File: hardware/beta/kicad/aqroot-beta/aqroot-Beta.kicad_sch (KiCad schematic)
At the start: 0 parts

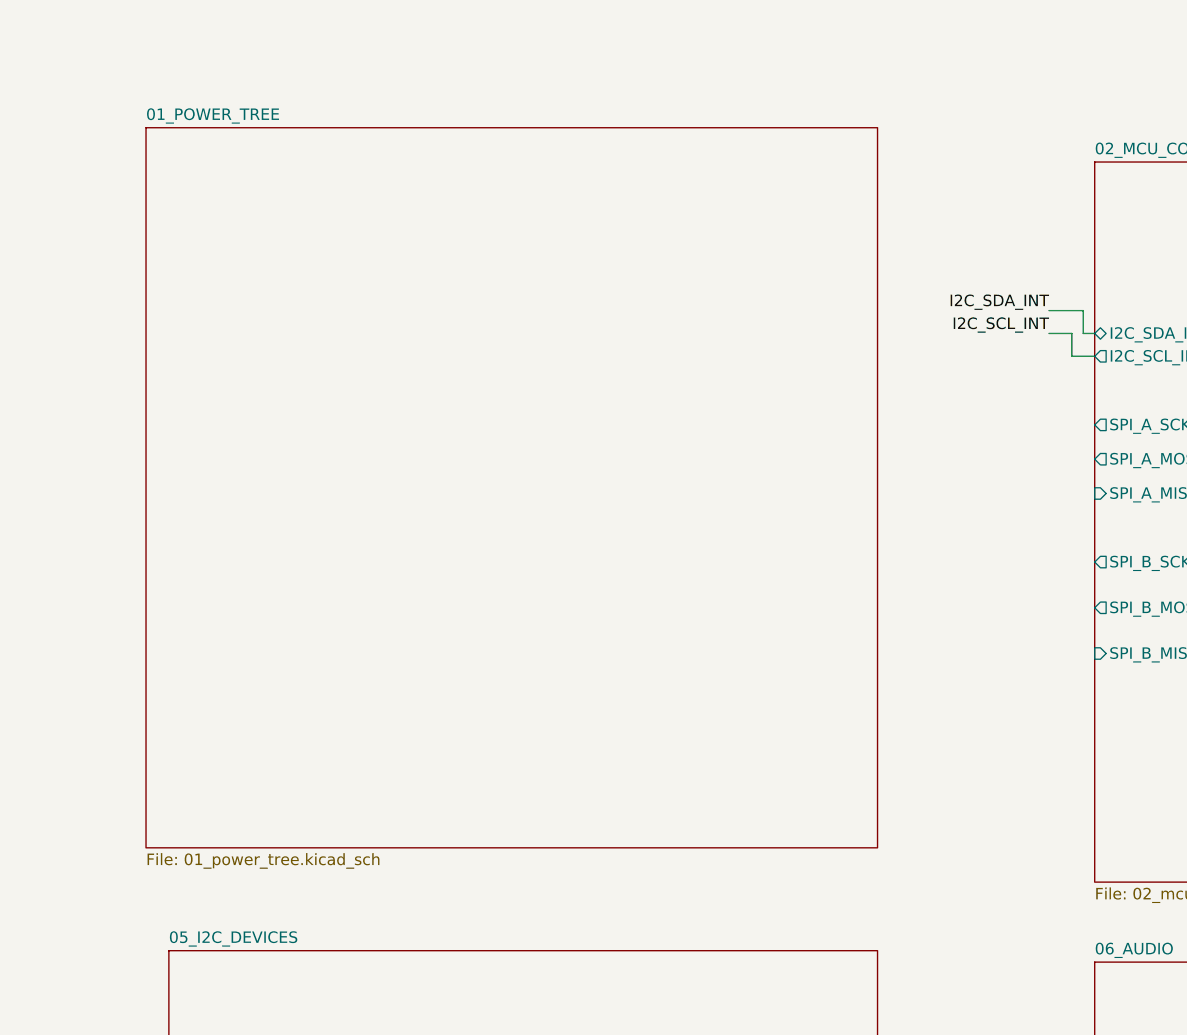
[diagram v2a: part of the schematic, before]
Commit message: AQROOT Beta: finish power-tree integration and add community-header connector map
01_POWER_TREE:
- Wire MAX17048 fuel gauge (U14): VDD/CELL to BAT_PROTECTED_P, GND/EP/CTG
  to GND, SCL to I2C_SCL_INT, SDA to I2C_SDA_INT, QSTRT no-connect.
- Add C36 bulk cap on BAT_PROTECTED_P and TP11 test point on MAX17048_ALRT_N.
- Add 8 hierarchical labels: USB_D_N_MCU, USB_D_P_MCU, I2C_SDA_INT,
  I2C_SCL_INT, NFC_5V_EN, NFC_5V_PA_PENDING, BQ25185_SYS, BAT_PROTECTED_P.

Root sheet:
- Import the 8 matching 01_POWER_TREE sheet pins and name six of them at
  root level, promoting BQ25185_SYS, BAT_PROTECTED_P, NFC_5V_EN,
  USB_D_N_MCU and USB_D_P_MCU from sheet-local to root nets.

09_COMMUNITY_HEADER:
- Add J5 (Conn_02x13_Odd_Even, PinHeader_2x13_P2.54mm_Vertical) with the
  full 26-pin map, plus orientation and 3.3V-only warning notes.

04_SPI_B_RADIOS_NFC:
- KiCad de-duplicated two colliding pin UUIDs on C19 (the file carried each
  UUID twice); included because it is a file-integrity fix, no design change.

Known incomplete, carried forward:
- Root sheet pins I2C_SDA_INT and NFC_5V_PA_PENDING are imported but not
  wired, so MAX17048 SDA sits on an isolated sheet-local net while SCL is
  bonded. Fuel-gauge I2C is not yet electrically complete.
- Community header nets are sheet-local only; 09_COMMUNITY_HEADER has no
  root sheet pins, and the 100R series / ESD parts named in its notes do
  not exist yet.
- Not ERC-clean and not fabrication-ready.

Co-Authored-By: Claude Opus 5 <noreply@anthropic.com>
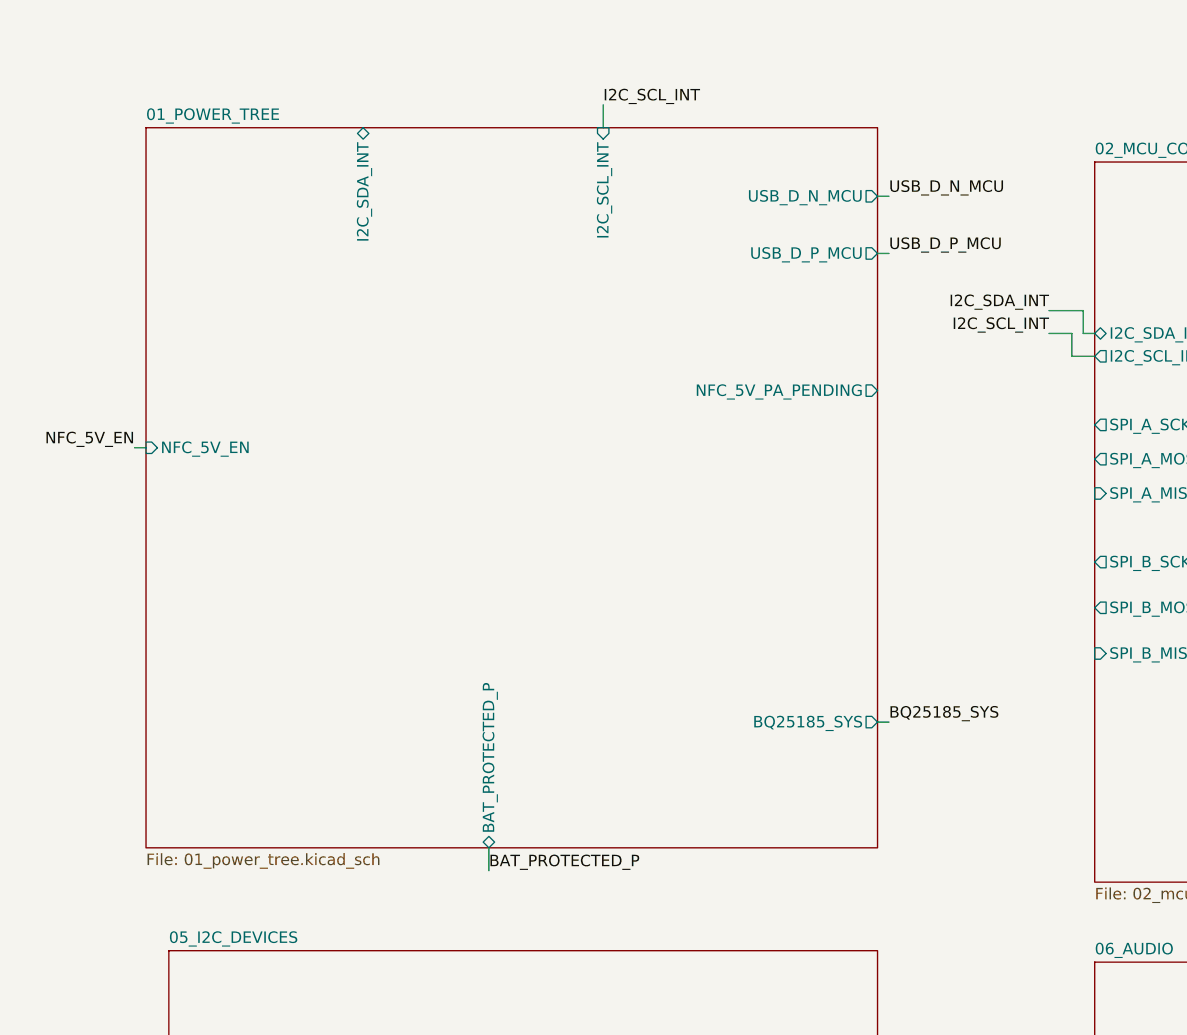
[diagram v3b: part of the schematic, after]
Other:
- sheet 01_POWER_TREE ports: added BAT_PROTECTED_P, BQ25185_SYS, I2C_SCL_INT, I2C_SDA_INT, NFC_5V_EN, NFC_5V_PA_PENDING, USB_D_N_MCU, USB_D_P_MCU; removed none
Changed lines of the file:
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@@
+	(wire
+		(pts
+			(xy 74.93 20.32) (xy 74.93 22.86)
+		)
+		(stroke
+			(width 0)
+			(type default)
+		)
+	)
 	(wire
 		(pts
@@
 	(wire
 		(pts
+			(xy 105.41 30.48) (xy 106.68 30.48)
+		)
+		(stroke
+			(width 0)
+			(type default)
+		)
+	)
+	(wire
+		(pts
 			(xy 128.27 45.72) (xy 128.27 43.18)
 		)
@@
 	(wire
 		(pts
+			(xy 105.41 88.9) (xy 106.68 88.9)
+		)
+		(stroke
+			(width 0)
+			(type default)
+		)
+	)
+	(wire
+		(pts
 			(xy 388.62 64.77) (xy 391.16 64.77)
 		)
@@
 	(wire
 		(pts
+			(xy 62.23 102.87) (xy 62.23 105.41)
+		)
+		(stroke
+			(width 0)
+			(type default)
+		)
+	)
+	(wire
+		(pts
 			(xy 388.62 60.96) (xy 391.16 60.96)
+		)
+		(stroke
+			(width 0)
+			(type default)
+		)
+	)
+	(wire
+		(pts
+			(xy 105.41 36.83) (xy 106.68 36.83)
+		)
+		(stroke
+			(width 0)
+			(type default)
+		)
+	)
+	(wire
+		(pts
+			(xy 22.86 58.42) (xy 24.13 58.42)
 		)
 		(stroke
@@
 		)
 	)
+	(label "NFC_5V_EN"
+		(at 22.86 58.42 180)
+		(effects
+			(font
+				(size 1.27 1.27)
+			)
+			(justify right bottom)
+		)
+	)
 	(label "DISP_CS_N"
 		(at 293.37 41.91 0)
@@
 		)
 	)
+	(label "USB_D_N_MCU"
+		(at 106.68 30.48 0)
+		(effects
+			(font
+				(size 1.27 1.27)
+			)
+			(justify left bottom)
+		)
+	)
 	(label "I2C_SDA_INT"
 		(at 124.46 43.18 180)
@@
 	)
 	(label "I2C_SCL_INT"
+		(at 74.93 20.32 0)
+		(effects
+			(font
+				(size 1.27 1.27)
+			)
+			(justify left bottom)
+		)
+	)
+	(label "BAT_PROTECTED_P"
+		(at 62.23 105.41 0)
+		(effects
+			(font
+				(size 1.27 1.27)
+			)
+			(justify left bottom)
+		)
+	)
+	(label "I2C_SCL_INT"
 		(at 124.46 45.72 180)
 		(effects
@@
 		)
 	)
+	(label "BQ25185_SYS"
+		(at 106.68 88.9 0)
+		(effects
+			(font
+				(size 1.27 1.27)
+			)
+			(justify left bottom)
+		)
+	)
 	(label "I2C_SDA_INT"
 		(at 223.52 91.44 180)
@@
 			)
 			(justify right bottom)
+		)
+	)
+	(label "USB_D_P_MCU"
+		(at 106.68 36.83 0)
+		(effects
+			(font
+				(size 1.27 1.27)
+			)
+			(justify left bottom)
 		)
 	)
@@
 			)
 		)
+		(pin "BAT_PROTECTED_P" bidirectional
+			(at 62.23 102.87 270)
+			(effects
+				(font
+					(size 1.27 1.27)
+				)
+				(justify left)
+			)
+		)
+		(pin "BQ25185_SYS" output
+			(at 105.41 88.9 0)
+			(effects
+				(font
+					(size 1.27 1.27)
+				)
+				(justify right)
+			)
+		)
+		(pin "I2C_SCL_INT" input
+			(at 74.93 22.86 90)
+			(effects
+				(font
+					(size 1.27 1.27)
+				)
+				(justify right)
+			)
+		)
+		(pin "I2C_SDA_INT" bidirectional
+			(at 48.26 22.86 90)
+			(effects
+				(font
+					(size 1.27 1.27)
+				)
+				(justify right)
+			)
+		)
+		(pin "NFC_5V_EN" input
+			(at 24.13 58.42 180)
+			(effects
+				(font
+					(size 1.27 1.27)
+				)
+				(justify left)
+			)
+		)
+		(pin "NFC_5V_PA_PENDING" output
+			(at 105.41 52.07 0)
+			(effects
+				(font
+					(size 1.27 1.27)
+				)
+				(justify right)
+			)
+		)
+		(pin "USB_D_N_MCU" output
+			(at 105.41 30.48 0)
+			(effects
+				(font
+					(size 1.27 1.27)
+				)
+				(justify right)
+			)
+		)
+		(pin "USB_D_P_MCU" output
+			(at 105.41 36.83 0)
+			(effects
+				(font
+					(size 1.27 1.27)
+				)
+				(justify right)
+			)
+		)

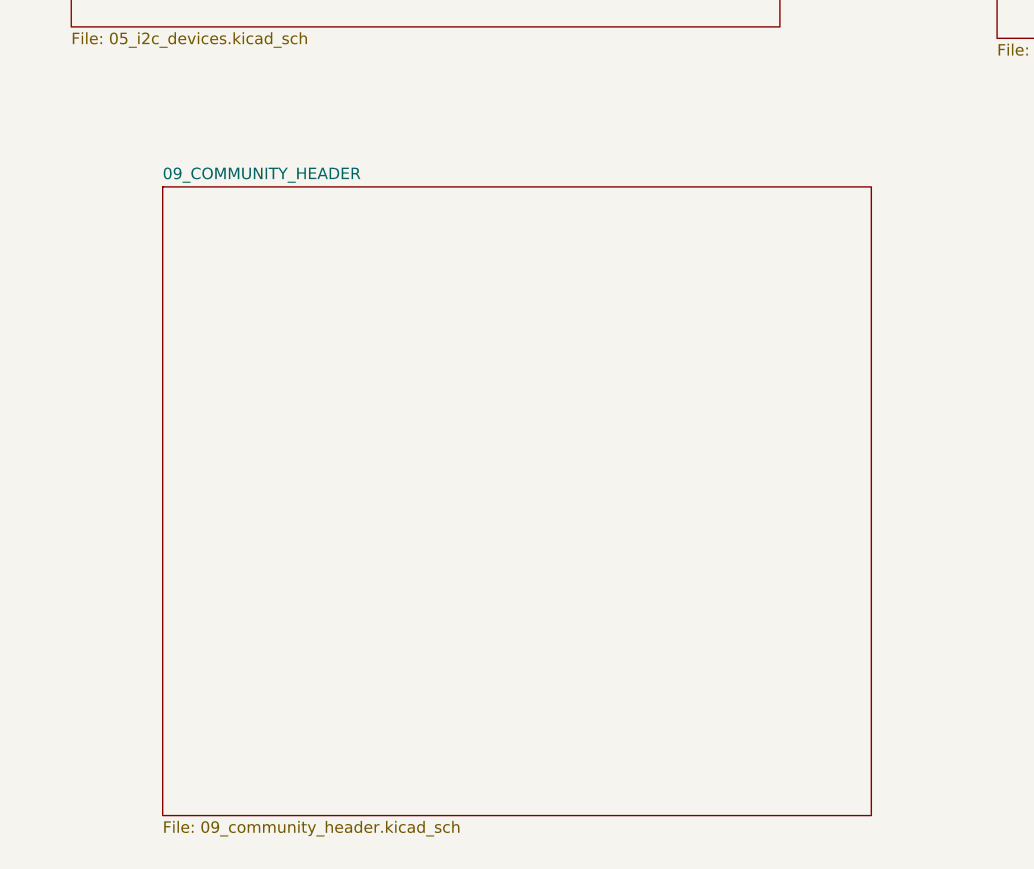
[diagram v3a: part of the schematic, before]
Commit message: AQROOT Beta: expose community-header internal hierarchy
09_COMMUNITY_HEADER:
- Add 20 hierarchical labels declaring the sheet's interface: XGPIO0-XGPIO14
  (bidirectional), I2C_SDA_INT (bidirectional), I2C_SCL_INT (input),
  ACC_PWR_EN (input), FAST_IO_U0TXD_ROOTPROBE_CS (input) and WAKE_INT_N
  (output). Purely additive: 220 insertions, 0 deletions.
- The existing connector-side local labels (XGPIO0_HDR-XGPIO14_HDR,
  I2C_SDA_EXT_HDR, I2C_SCL_EXT_HDR, FAST_IO_GPIO43_HDR, WAKE_ATTN_N_HDR,
  ACC_3V3_SW) are untouched.

Root sheet:
- Add the 20 matching sheet pins to the 09_COMMUNITY_HEADER sheet symbol.

This exposes the interface only. It does not connect anything:

- All 20 new root sheet pins are PLACED BUT UNWIRED. None carries a root
  wire, none has a matching root label, and none shares a net with any
  other sheet pin. Root pins still require wiring.
- The 20 new hierarchical labels inside 09 are likewise not attached to any
  wire, so they do not yet meet the *_HDR connector nets.
- J5 protection circuitry is not captured yet. The sheet notes call for
  100R series resistors and connector-side ESD on every XGPIO line; those
  parts do not exist, and they are what should eventually bridge XGPIO<n>
  to XGPIO<n>_HDR.

Verified with kicad-cli netlist export: this commit changes zero
connectivity. 145 nets and 433 pins before and after, with no pin changing
net. ERC rises 217 -> 257 violations, exactly +20 pin_not_connected and
+20 label_dangling, one of each per declared signal.

Not ERC-clean. Not fabrication-ready.

Co-Authored-By: Claude Opus 5 <noreply@anthropic.com>
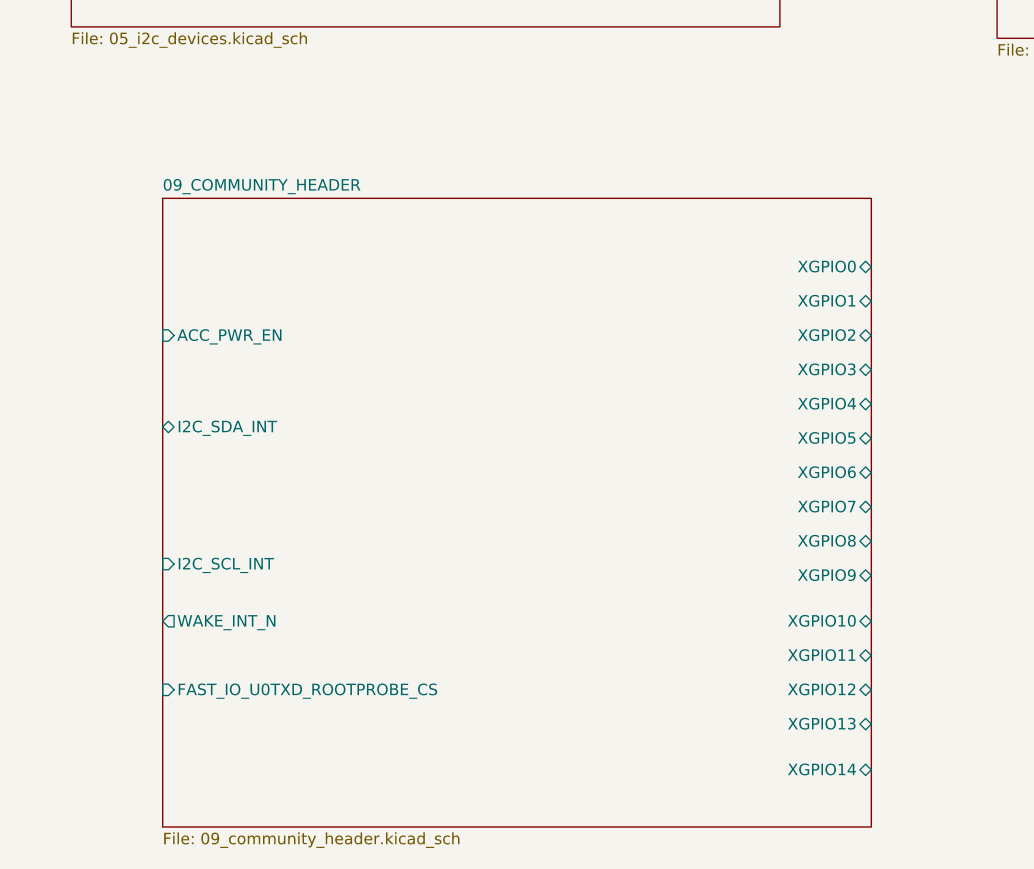
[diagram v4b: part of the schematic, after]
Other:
- sheet 09_COMMUNITY_HEADER ports: added ACC_PWR_EN, FAST_IO_U0TXD_ROOTPROBE_CS, I2C_SCL_INT, I2C_SDA_INT, WAKE_INT_N, XGPIO0, XGPIO1, XGPIO10, XGPIO11, XGPIO12, XGPIO13, XGPIO14, XGPIO2, XGPIO3, XGPIO4, XGPIO5, XGPIO6, XGPIO7, XGPIO8, XGPIO9; removed none
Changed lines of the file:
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@@
+	(wire
+		(pts
+			(xy 223.52 57.15) (xy 226.06 57.15)
+		)
+		(stroke
+			(width 0)
+			(type default)
+		)
+	)
+	(wire
+		(pts
+			(xy 320.04 144.78) (xy 322.58 144.78)
+		)
+		(stroke
+			(width 0)
+			(type default)
+		)
+	)
+	(wire
+		(pts
+			(xy 320.04 77.47) (xy 322.58 77.47)
+		)
+		(stroke
+			(width 0)
+			(type default)
+		)
+	)
+	(wire
+		(pts
+			(xy 223.52 165.1) (xy 226.06 165.1)
+		)
+		(stroke
+			(width 0)
+			(type default)
+		)
+	)
 	(wire
 		(pts
@@
 	(wire
 		(pts
-			(xy 223.52 57.15) (xy 226.06 57.15)
-		)
-		(stroke
-			(width 0)
-			(type default)
-		)
-	)
-	(wire
-		(pts
-			(xy 320.04 77.47) (xy 322.58 77.47)
-		)
-		(stroke
-			(width 0)
-			(type default)
-		)
-	)
-	(wire
-		(pts
-			(xy 223.52 165.1) (xy 226.06 165.1)
-		)
-		(stroke
-			(width 0)
-			(type default)
-		)
-	)
-	(wire
-		(pts
 			(xy 200.66 151.13) (xy 203.2 151.13)
 		)
@@
 	(wire
 		(pts
-			(xy 320.04 144.78) (xy 322.58 144.78)
-		)
-		(stroke
-			(width 0)
-			(type default)
-		)
-	)
-	(wire
-		(pts
 			(xy 128.27 43.18) (xy 124.46 43.18)
 		)
@@
 	(wire
 		(pts
+			(xy 320.04 149.86) (xy 322.58 149.86)
+		)
+		(stroke
+			(width 0)
+			(type default)
+		)
+	)
+	(wire
+		(pts
 			(xy 223.52 78.74) (xy 226.06 78.74)
 		)
@@
 		(pts
 			(xy 223.52 91.44) (xy 226.06 91.44)
-		)
-		(stroke
-			(width 0)
-			(type default)
-		)
-	)
-	(wire
-		(pts
-			(xy 320.04 149.86) (xy 322.58 149.86)
 		)
 		(stroke
@@
 	)
 	(sheet
-		(at 36.83 205.74)
+		(at 36.83 207.01)
 		(size 78.74 69.85)
 		(exclude_from_sim no)
@@
 		)
 		(property "Sheetname" "09_COMMUNITY_HEADER"
-			(at 36.83 205.0284 0)
+			(at 36.83 206.2984 0)
 			(show_name no)
 			(do_not_autoplace no)
@@
 		)
 		(property "Sheetfile" "09_community_header.kicad_sch"
-			(at 36.83 276.1746 0)
+			(at 36.83 277.4446 0)
 			(show_name no)
 			(do_not_autoplace no)
@@
 			)
 		)
+		(pin "ACC_PWR_EN" input
+			(at 36.83 222.25 180)
+			(effects
+				(font
+					(size 1.27 1.27)
+				)
+				(justify left)
+			)
+		)
+		(pin "FAST_IO_U0TXD_ROOTPROBE_CS" input
+			(at 36.83 261.62 180)
+			(effects
+				(font
+					(size 1.27 1.27)
+				)
+				(justify left)
+			)
+		)
+		(pin "I2C_SCL_INT" input
+			(at 36.83 247.65 180)
+			(effects
+				(font
+					(size 1.27 1.27)
+				)
+				(justify left)
+			)
+		)
+		(pin "I2C_SDA_INT" bidirectional
+			(at 36.83 232.41 180)
+			(effects
+				(font
+					(size 1.27 1.27)
+				)
+				(justify left)
+			)
+		)
+		(pin "WAKE_INT_N" output
+			(at 36.83 254 180)
+			(effects
+				(font
+					(size 1.27 1.27)
+				)
+				(justify left)
+			)
+		)
+		(pin "XGPIO0" bidirectional
+			(at 115.57 214.63 0)
+			(effects
+				(font
+					(size 1.27 1.27)
+				)
+				(justify right)
+			)
+		)
+		(pin "XGPIO1" bidirectional
+			(at 115.57 218.44 0)
+			(effects
+				(font
+					(size 1.27 1.27)
+				)
+				(justify right)
+			)
+		)
+		(pin "XGPIO2" bidirectional
+			(at 115.57 222.25 0)
+			(effects
+				(font
+					(size 1.27 1.27)
+				)
+				(justify right)
+			)
+		)
+		(pin "XGPIO3" bidirectional
+			(at 115.57 226.06 0)
+			(effects
+				(font
+					(size 1.27 1.27)
+				)
+				(justify right)
+			)
+		)
+		(pin "XGPIO4" bidirectional
+			(at 115.57 229.87 0)
+			(effects
+				(font
+					(size 1.27 1.27)
+				)
+				(justify right)
+			)
+		)
+		(pin "XGPIO5" bidirectional
+			(at 115.57 233.68 0)
+			(effects
+				(font
+					(size 1.27 1.27)
+				)
+				(justify right)
+			)
+		)
+		(pin "XGPIO6" bidirectional
+			(at 115.57 237.49 0)
+			(effects
+				(font
+					(size 1.27 1.27)
+				)
+				(justify right)
+			)
+		)
+		(pin "XGPIO7" bidirectional
+			(at 115.57 241.3 0)
+			(effects
+				(font
+					(size 1.27 1.27)
+				)
+				(justify right)
+			)
+		)
+		(pin "XGPIO8" bidirectional
+			(at 115.57 245.11 0)
+			(effects
+				(font
+					(size 1.27 1.27)
+				)
+				(justify right)
+			)
+		)
+		(pin "XGPIO9" bidirectional
+			(at 115.57 248.92 0)
+			(effects
+				(font
+					(size 1.27 1.27)
+				)
+				(justify right)
+			)
+		)
+		(pin "XGPIO10" bidirectional
+			(at 115.57 254 0)
+			(effects
+				(font
+					(size 1.27 1.27)
+				)
+				(justify right)
+			)
+		)
+		(pin "XGPIO11" bidirectional
+			(at 115.57 257.81 0)
+			(effects
+				(font
+					(size 1.27 1.27)
+				)
+				(justify right)
+			)
+		)
+		(pin "XGPIO12" bidirectional
+			(at 115.57 261.62 0)
+			(effects
+				(font
+					(size 1.27 1.27)
+				)
+				(justify right)
+			)
+		)
+		(pin "XGPIO13" bidirectional
+			(at 115.57 265.43 0)
+			(effects
+				(font
+					(size 1.27 1.27)
+				)
+				(justify right)
+			)
+		)
+		(pin "XGPIO14" bidirectional
+			(at 115.57 270.51 0)
+			(effects
+				(font
+					(size 1.27 1.27)
+				)
+				(justify right)
+			)
+		)
